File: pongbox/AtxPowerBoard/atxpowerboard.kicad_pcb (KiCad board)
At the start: 2 copper layers, 75.6 x 43.2 mm, 15 parts, among them P1 CONN_10X2, P2 5V, P3 12V, P4 CONN_1, P5 CONN_1, P6 CONN_1, P7 CONN_1, P8 CONN_1, P9 CONN_1

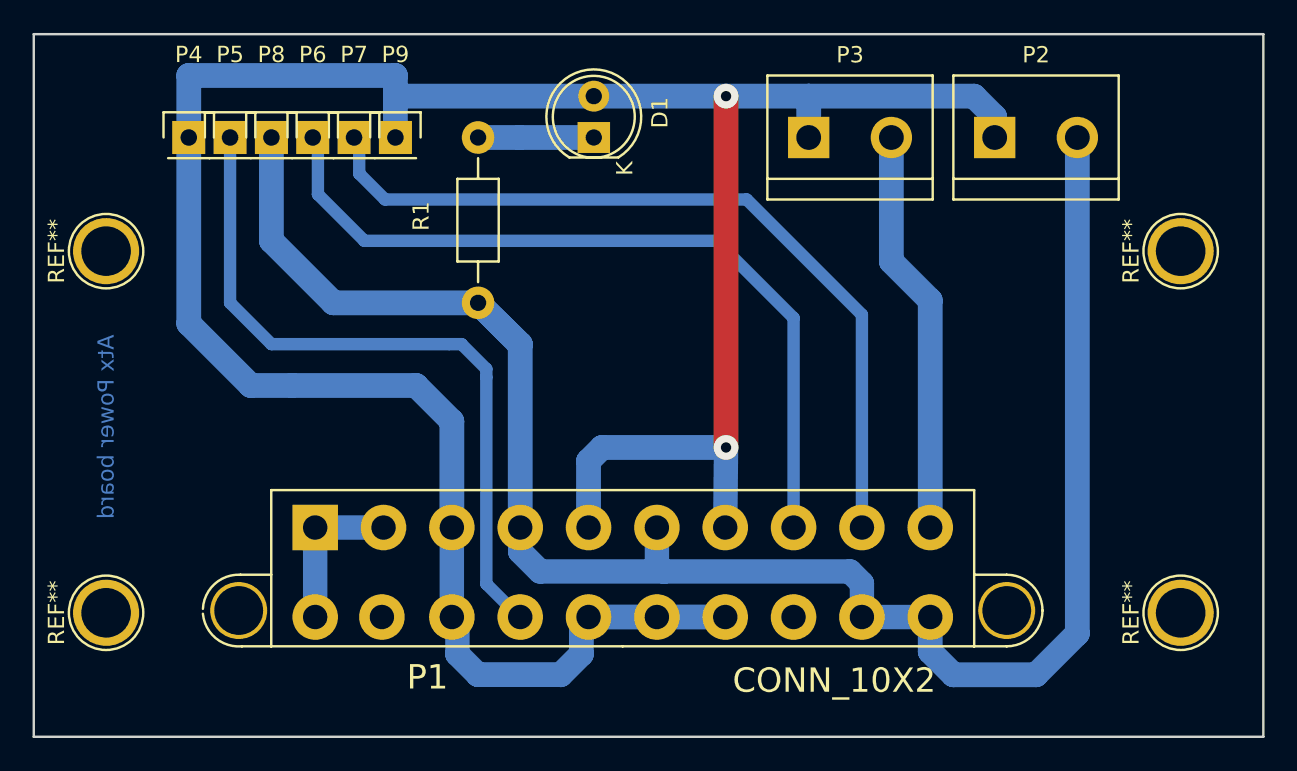
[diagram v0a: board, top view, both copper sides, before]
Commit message: ajust dimentions de la carte
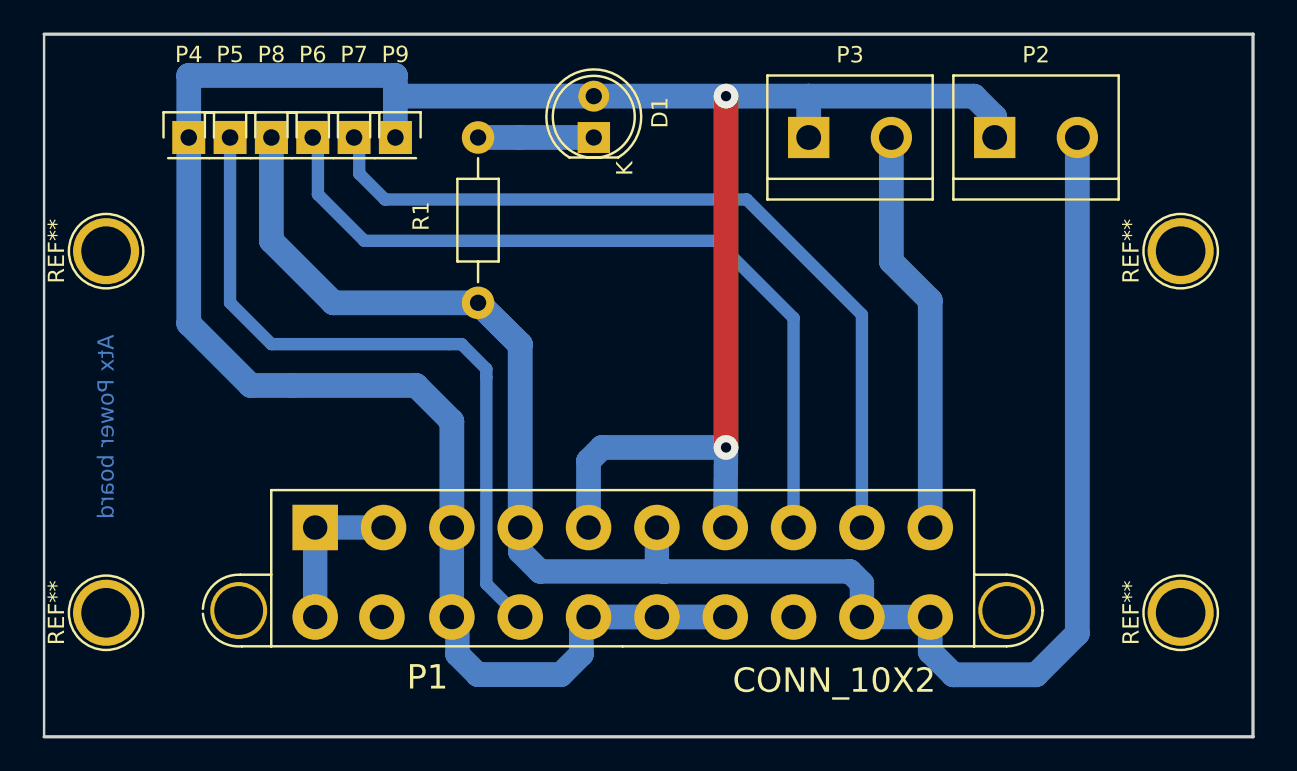
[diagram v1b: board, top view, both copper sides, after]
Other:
- board size 75.6 x 43.2 mm -> 74.3 x 43.2 mm
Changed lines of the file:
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@@
-(kicad_pcb (version 4) (host pcbnew 0.201509040901+6154~29~ubuntu14.04.1-product)
+(kicad_pcb (version 4) (host pcbnew 0.201509211831+6205~30~ubuntu14.04.1-product)
   (general
     (links 24)
     (no_connects 0)
-    (area 79.299999 77.394999 155.015001 120.725001)
+    (area 79.593 71.585 172.463334 120.750001)
     (thickness 1.6)
     (drawings 5)
@@
     (visible_elements 7FFFFFFF)
     (pcbplotparams
-      (layerselection 0x00020_80000000)
+      (layerselection 0x00000_80000000)
       (usegerberextensions false)
       (excludeedgelayer false)
@@
       (outputformat 2)
       (mirror false)
-      (drillshape 0)
+      (drillshape 1)
       (scaleselection 1)
       (outputdirectory ci/))
@@
     (pad 1 thru_hole circle (at 0 0 90) (size 4.064 4.064) (drill 3.048) (layers *.Cu *.Mask F.SilkS))
   )
-  (gr_line (start 154.94 120.65) (end 79.375 120.65) (angle 90) (layer Edge.Cuts) (width 0.15))
-  (gr_line (start 154.94 77.47) (end 154.94 120.65) (angle 90) (layer Edge.Cuts) (width 0.15))
-  (gr_line (start 79.375 77.47) (end 154.94 77.47) (angle 90) (layer Edge.Cuts) (width 0.15))
-  (gr_line (start 79.375 120.65) (end 79.375 77.47) (angle 90) (layer Edge.Cuts) (width 0.15))
+  (gr_line (start 80.01 77.47) (end 154.305 77.47) (angle 90) (layer Edge.Cuts) (width 0.2))
+  (gr_line (start 80.01 120.65) (end 154.305 120.65) (angle 90) (layer Edge.Cuts) (width 0.2))
+  (gr_line (start 154.305 120.65) (end 154.305 77.47) (angle 90) (layer Edge.Cuts) (width 0.2))
+  (gr_line (start 80.01 77.47) (end 80.01 120.65) (angle 90) (layer Edge.Cuts) (width 0.15))
   (gr_text "Atx Power board" (at 83.82 101.6 90) (layer B.Cu)
     (effects (font (size 1 1) (thickness 0.25)) (justify mirror))
